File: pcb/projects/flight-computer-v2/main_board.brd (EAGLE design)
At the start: 127 x 64.4 mm, 110 parts, among them J1 B4B-PH-K-S(LF)(SN), J2 B4B-PH-K-S(LF)(SN), J3 B4B-PH-K-S(LF)(SN), J4 B4B-PH-K-S(LF)(SN), J5 B4B-PH-K-S(LF)(SN), J6 B4B-PH-K-S(LF)(SN), J7 104031-0811, J8 B4B-PH-K-S(LF)(SN), J9 U.FL-R-SMT(10), U1 COM-13909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

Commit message: update libraries and v2 flight comp
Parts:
- added JP5: (no value), pinhead:1X02
- added JP6: (no value), pinhead:1X04
- added JP7: (no value), pinhead:1X03
- added LED1, LED2, LED3, LED4: (no value), adafruit:CHIPLED_0603
- added R10, R11, R12, R27: (no value), rcl:R0603
- added U3: IRF7313PBF, COM-13909:SO-8
- moved JP2 4.71 mm to (2.92, 46.0)
- moved J5 4.47 mm to (7.37, 46.0)
- moved J3 1.27 mm to (52.1, 24.1)
- moved JP1 1.27 mm to (25.4, 19.1)
- moved JP3 1.27 mm to (30.5, 39.4)
- moved C23 0.85 mm to (108.7, 42.3)
- moved R8 0.63 mm to (39.4, 42.5)
- moved C27 0.38 mm to (110.5, 29.6)
- moved C26 0.25 mm to (95.6, 15.0)
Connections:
- removed net GATE_RADIO: JP1.12
- new net BOOTN: JP6.3, U$4.6
- new net EXT_INT: JP1.12, JP5.1
- new net H3_INT1: JP7.2, U2.11
- new net H3_INT2: JP7.3, U2.9
- new net HINTN: JP6.4, U$4.5
- new net N$19: LED1.A, R10.2
- new net PS1: JP6.2, U$4.7
- new net VIN_GND: J5.1, U3.5, U3.6, U3.7, U3.8
- net 3V32_CTRL: now also R27.1
- net FSM300_RESET: now also JP6.1
- net GATE_IRIDIUM: now also R10.1, U3.2, U3.4
- net GATE_PI: now also R11.1
- net GATE_SPEC: now also R12.1
- net GND: now also JP5.2, LED1.C, LED2.C, LED3.C, LED4.C, U$4.9, U3.1, U3.3; no longer J5.2
- net ICM_INT: now also JP7.1
- net N$33: now also LED2.A, R11.2; no longer U$4.5
- net N$36: now also LED3.A, R12.2; no longer U$4.6
- net N$37: now also LED4.A, R27.2; no longer U$4.7
- net VIN: now also J5.2; no longer J5.1
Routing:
- net FSM300_RESET: track 0.00 -> 55.2 mm
- net GND: track 149.5 -> 191.7 mm, vias 85 -> 94
- net GATE_IRIDIUM: track 29.5 -> 63.0 mm, vias 1 -> 2
- net H3_INT1: track 0.00 -> 16.1 mm, vias 0 -> 1
- net PS1: track 0.00 -> 15.6 mm
- net BOOTN: track 0.00 -> 15.5 mm
- net HINTN: track 0.00 -> 15.3 mm
- net H3_INT2: track 0.00 -> 15.2 mm, vias 0 -> 1
- net ICM_INT: track 0.00 -> 14.8 mm
- net EXT_INT: track 0.00 -> 14.2 mm
- net GATE_SPEC: track 35.3 -> 48.5 mm, vias 1 -> 2
- net VIN_GND: track 0.00 -> 10.8 mm
- net N$33: track 0.00 -> 4.75 mm
- net SCK: track 89.9 -> 85.9 mm
- net 3V3: track 441.0 -> 437.9 mm
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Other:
- outline, holes or cut-outs redrawn
- board text added: "13"
- board text added: "14"
- board text added: "14 EXT_INT 15 RX4 16 TGPS 17 RGPS 18 TX4 19 SD_CS 25 SCK 24 MOSI 23 MISO 0 RX1 1 TX1 4 GATE_PI"
- board text added: "21"
- board text added: "4"
- board text added: "ACT"
- board text added: "BOOTN"
- board text added: "H3 INT 1 H3 INT 2 ICM INT"
- board text added: "INT"
- board text added: "KREPE Flight Computer v2.0"
- board text added: "Matt Ruffner, Evan Wells, Kirsten Ford, Bruno Tacchi, Dr. Alexandre Martin Dr. Bill Smith Dr. Savio Poovathingal"
- board text added: "NEOPIXEL 8 VBAT/2 A6 RIRI 13 TIRI 12 GATE_IR 11 RADIO_SS 10 RADIO_RST 9 3V32_CTRL 6 GATE_SPEC 5 SCL 22 SDA 21"
- board text added: "PS1"
- board text added: "RST"
- board text added: "U11 3v3 source"
- board text added: "VBUS to 5V"
- board text added: "VIN - VIN + VBAT + VBAT -"
- board text added: "feather"
- board text removed: "KREPE-2 Flight Computer"
- board text removed: "Matt Ruffner, Evan Wells, Kirsten Ford, Bruno Tacci, Dr. Alexandre Martin Dr. Bill Smith Dr. Savio Poovathingal"
- board text removed: "U11 source"
- board text removed: "VIN GND VBAT GND"
- board text removed: "feat."

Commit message: v2 cam files, renderings, and datasheets
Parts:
- added C2: 0.1uF, rcl:C0603
- moved J3 3.81 mm to (52.1, 27.9)
- moved C7 1.98 mm to (36.8, 53.6), turned to 180 degrees
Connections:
- net GND: now also C2.1, C7.1
- net N$11: now also C7.2; no longer C7.1
- net N$9: now also C2.2; no longer C7.2
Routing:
- net SDA: track 207.6 -> 203.1 mm
- net RADIO_SS: track 58.7 -> 54.3 mm
- net RADIO_RESET: track 55.2 -> 51.6 mm
- net SCL: track 189.0 -> 186.7 mm
- net GND: track 191.7 -> 194.0 mm, vias 94 -> 95
- net N$11: track 3.65 -> 4.35 mm
- net 3V3: track 437.9 -> 438.4 mm
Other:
- board text added: "Matt Ruffner, Evan Wells, Kirsten Ford, Bruno Tacchi, Logan Craig, Dr. Alexandre Martin Dr. Bill Smith Dr. Savio Poovathingal"
- board text removed: "Matt Ruffner, Evan Wells, Kirsten Ford, Bruno Tacchi, Dr. Alexandre Martin Dr. Bill Smith Dr. Savio Poovathingal"

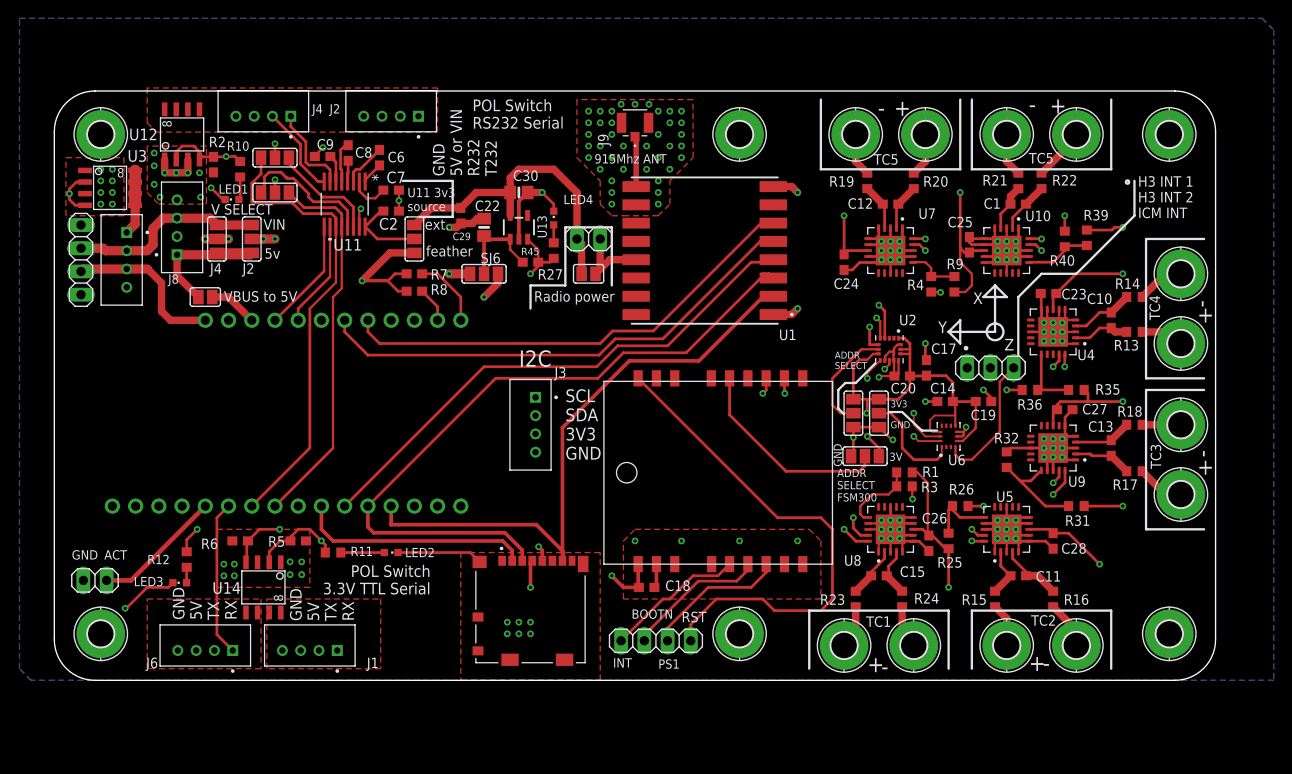
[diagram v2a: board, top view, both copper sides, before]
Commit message: add ssr to flight computer. add to hardware manual
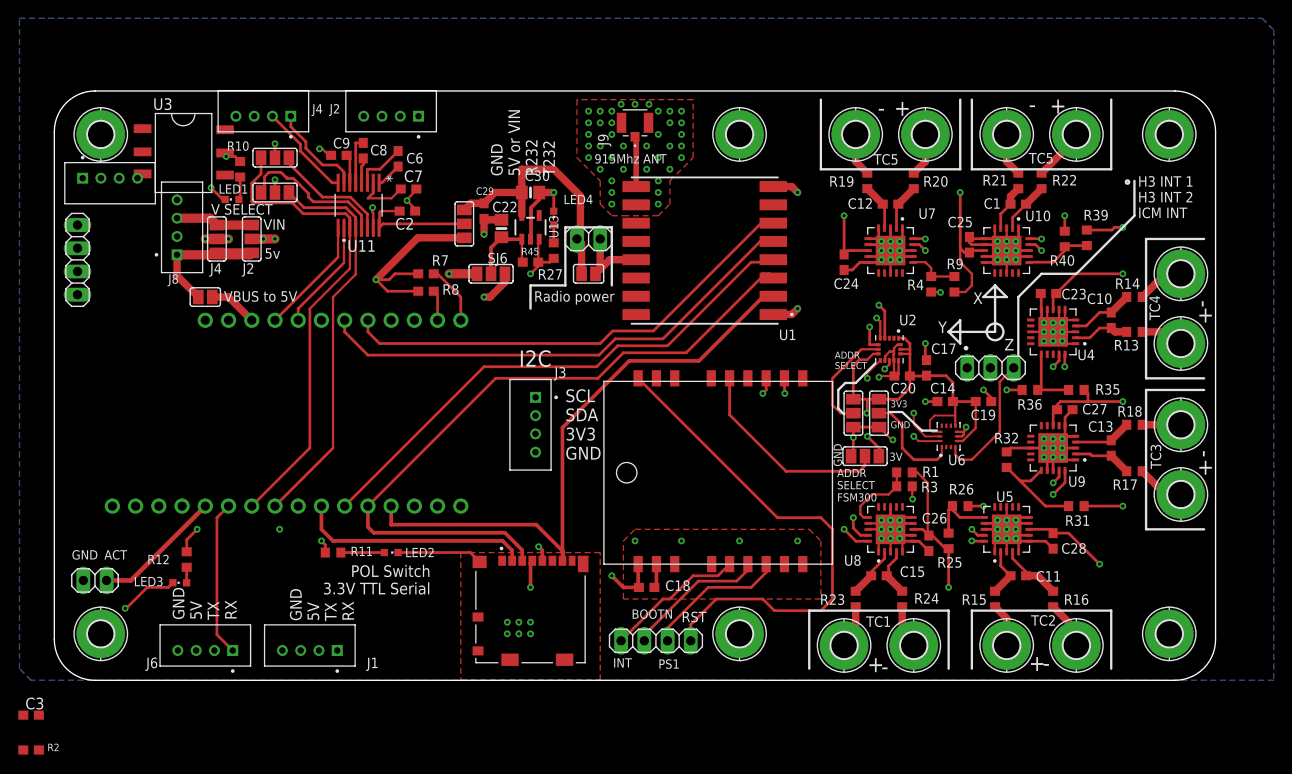
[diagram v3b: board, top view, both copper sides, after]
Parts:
- removed R5, R6: 100k, microbuilder:0603-NO
- removed U12, U14: IRF7313PBF, COM-13909:SO-8
- added C3: 0.1uF, rcl:C0603
- R2: value 100k -> 288
- U3: value IRF7313PBF -> AQV252G; device COM-13909:SO-8 -> AQV252G:SOP6
- moved R2 67.0 mm to (-2.54, -7.62), turned to 0 degrees
- moved J5 8.48 mm to (6.10, 54.4), turned to 180 degrees
- moved U3 7.89 mm to (14.0, 53.3)
- moved SJ8 5.71 mm to (44.8, 49.9)
- moved C29 2.59 mm to (47.0, 51.3)
- moved C6 2.04 mm to (37.6, 57.0)
- moved C22 1.91 mm to (48.9, 49.4)
- moved C7 1.91 mm to (38.7, 53.7)
- moved C9 1.78 mm to (31.1, 57.4)
- moved C2 1.78 mm to (38.6, 51.3)
- moved C8 1.67 mm to (33.8, 57.9)
- moved U11 1.53 mm to (33.3, 51.9)
- moved C30 1.27 mm to (52.1, 53.3)
- moved R7 1.27 mm to (40.6, 44.5)
- moved R8 1.27 mm to (40.6, 42.5)
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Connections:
- removed net VIN_GND: J5.1, U3.5, U3.6, U3.7, U3.8
- new net DIO0: U1.14
- new net N$18: C3.2, R2.2, U3.1
- new net VIN_PRE: J5.2, U3.6
- net GATE_IRIDIUM: no longer U12.2, U12.4, U3.2, U3.4
- net GATE_PI: no longer R5.1, U14.2
- net GATE_SPEC: no longer R6.1, U14.4
- net GND: now also C3.1, J5.1, U3.2; no longer R2.2, R5.2, R6.2, U12.1, U12.3, U14.1, U14.3, U3.1, U3.3
- net GND_IRIDIUM: no longer U12.5, U12.6, U12.7, U12.8
- net GND_PI: no longer U14.7, U14.8
- net GND_SPEC: no longer U14.5, U14.6
- net VIN: now also U3.4; no longer J5.2
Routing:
- net GATE_IRIDIUM: track 63.0 -> 24.0 mm, vias 2 -> 1
- net VBAT: track 53.4 -> 36.3 mm
- net VIN: track 21.6 -> 8.48 mm
- net VIN_GND: track 10.8 -> 0.00 mm
- net GATE_PI: track 31.3 -> 22.6 mm
- net GATE_SPEC: track 48.5 -> 42.1 mm
- net 3V3: track 438.4 -> 444.1 mm
- net GND: track 194.0 -> 188.4 mm, vias 95 -> 70
- net N$9: track 8.16 -> 13.5 mm
- net 3V32: track 33.9 -> 28.6 mm
- net TGPS: track 50.5 -> 52.7 mm
- net RGPS: track 41.7 -> 43.6 mm
- net N$11: track 4.35 -> 5.96 mm
- net R232_GPS: track 14.9 -> 16.3 mm
- net SDA: track 203.1 -> 201.8 mm
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- removed copper zone on layer 1, net GND_IRIDIUM
- removed copper zone on layer 1, net GND_PI
- removed copper zone on layer 1, net GND_SPEC
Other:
- board text removed: "POL Switch RS232 Serial"
- board text removed: "U11 3v3 source"
- board text removed: "ext."
- board text removed: "feather"
